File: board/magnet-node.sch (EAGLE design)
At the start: 30 parts, among them X1 SMA-142-0701-801/806, X2 SMA-142-0711-821/826

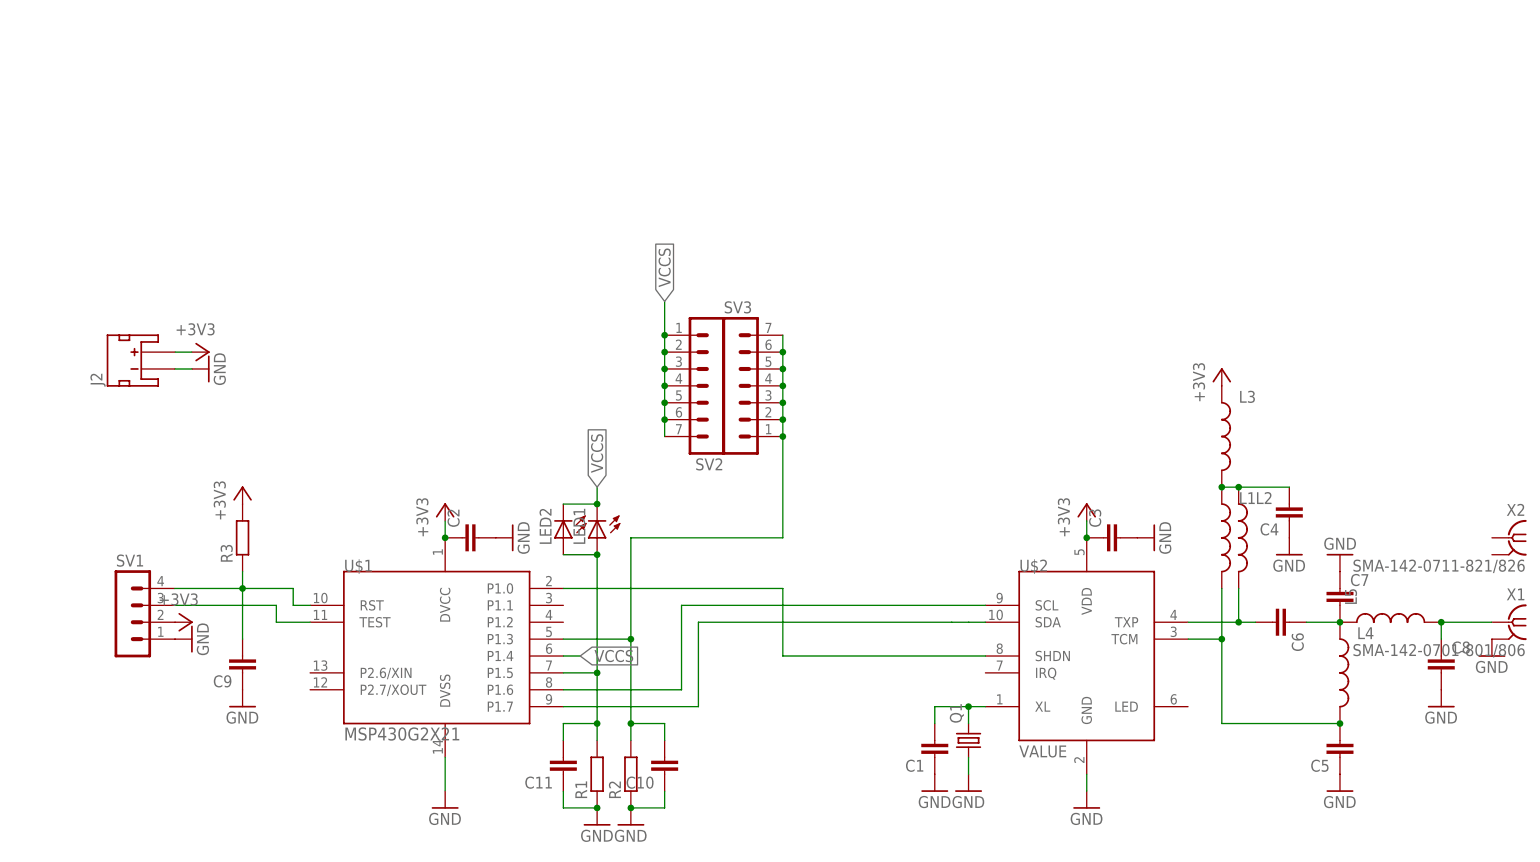
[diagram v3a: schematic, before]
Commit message: added temp/humid sensor
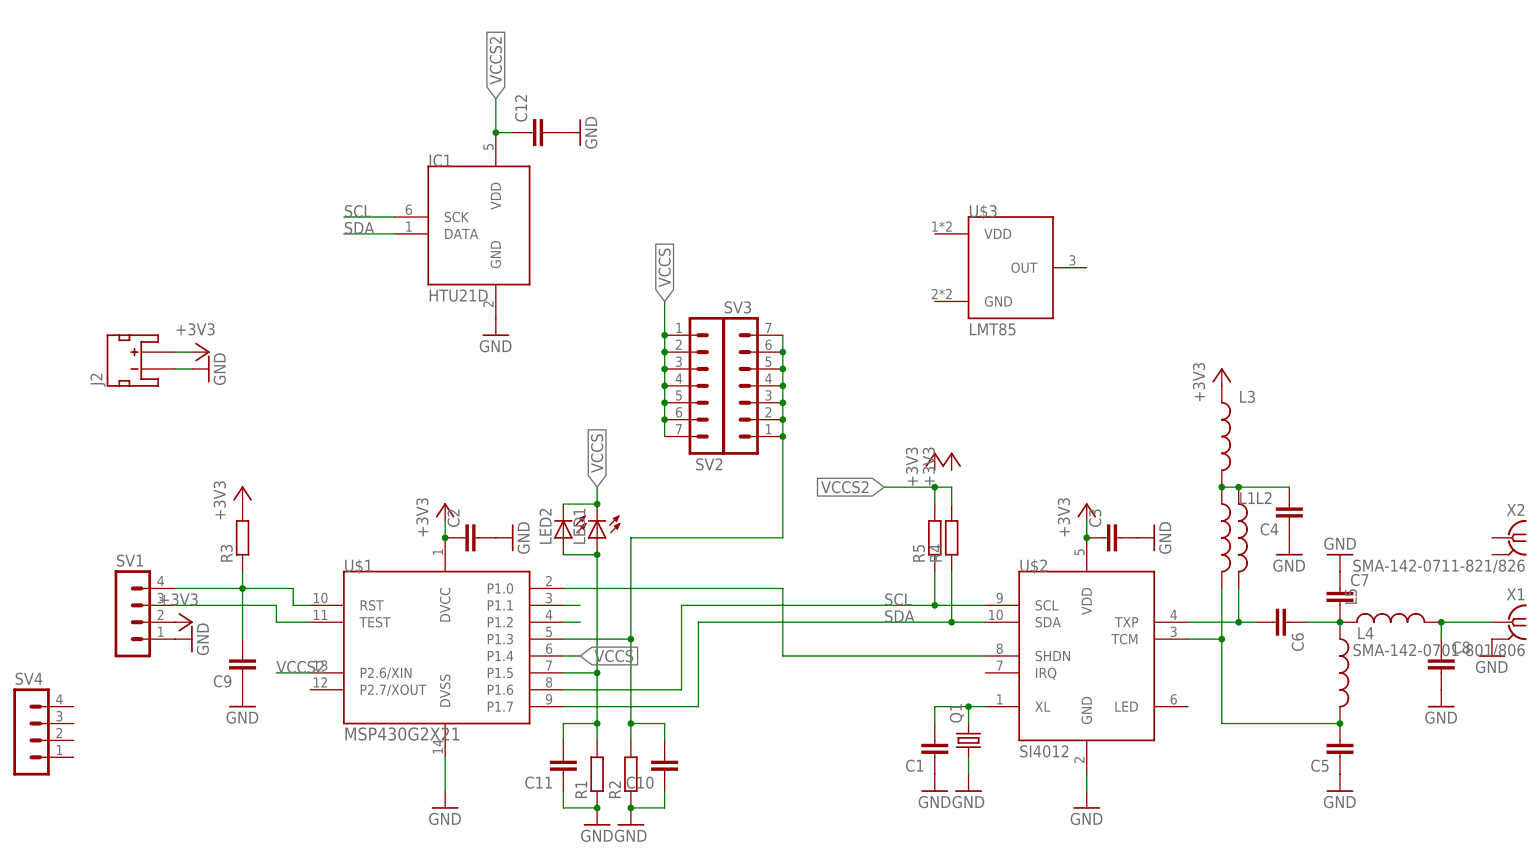
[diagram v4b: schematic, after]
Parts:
- added C12: (no value), rcl:C-EUC0603
- added IC1: HTU21D, Mine:HTU21D
- added R4, R5: (no value), rcl:R-EU_R0603
- added SV4: (no value), Mine:MA04-1E
- added U$3: LMT85, Mine:LMT85
- SV1: device con-lstb:MA04-1 -> Mine:MA04-1E
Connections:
- removed net N$3: U$1.P1.6, U$2.SCL
- removed net N$6: U$1.P1.7, U$2.SDA
- new net N$11: U$1.P1.1
- new net N$14: U$1.P1.2
- new net SCL: IC1.SCK, R5.1, U$1.P1.6, U$2.SCL
- new net SDA: IC1.DATA, R4.1, U$1.P1.7, U$2.SDA
- new net VCCS2: C12.1, IC1.VDD, R4.2, R5.2, U$1.P2.6/XIN
- net GND: now also C12.2, IC1.GND
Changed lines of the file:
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@@
 <part name="GND3" library="supply1" deviceset="GND" device=""/>
 <part name="GND4" library="supply1" deviceset="GND" device=""/>
-<part name="SV1" library="con-lstb" deviceset="MA04-1" device=""/>
+<part name="SV1" library="Mine" deviceset="MA04-1" device="E"/>
 <part name="+3V3" library="supply1" deviceset="+3V3" device=""/>
 <part name="GND5" library="supply1" deviceset="GND" device=""/>
@@
 <part name="X2" library="con-coax" deviceset="SMA-" device="142-0711-821/826"/>
 <part name="LED2" library="led" deviceset="LED" device="SMT1206"/>
+<part name="U$3" library="Mine" deviceset="LMT85" device=""/>
+<part name="IC1" library="Mine" deviceset="HTU21D" device=""/>
+<part name="SV4" library="Mine" deviceset="MA04-1" device="E"/>
+<part name="GND17" library="supply1" deviceset="GND" device=""/>
+<part name="C12" library="rcl" deviceset="C-EU" device="C0603"/>
+<part name="GND18" library="supply1" deviceset="GND" device=""/>
+<part name="R4" library="rcl" deviceset="R-EU_" device="R0603"/>
+<part name="R5" library="rcl" deviceset="R-EU_" device="R0603"/>
+<part name="+3V7" library="supply1" deviceset="+3V3" device=""/>
+<part name="+3V9" library="supply1" deviceset="+3V3" device=""/>
 </parts>
 <sheets>
@@
 <instance part="X2" gate="G1" x="205.74" y="58.42" rot="MR0"/>
 <instance part="LED2" gate="G$1" x="63.5" y="58.42" rot="R180"/>
+<instance part="U$3" gate="G$1" x="134.62" y="99.06"/>
+<instance part="IC1" gate="G$1" x="48.26" y="104.14"/>
+<instance part="SV4" gate="1" x="-17.78" y="30.48"/>
+<instance part="GND17" gate="1" x="53.34" y="88.9"/>
+<instance part="C12" gate="G$1" x="58.42" y="119.38" rot="R90"/>
+<instance part="GND18" gate="1" x="66.04" y="119.38" rot="R90"/>
+<instance part="R4" gate="G$1" x="121.92" y="58.42" rot="R90"/>
+<instance part="R5" gate="G$1" x="119.38" y="58.42" rot="R90"/>
+<instance part="+3V7" gate="G$1" x="121.92" y="71.12"/>
+<instance part="+3V9" gate="G$1" x="119.38" y="71.12"/>
 </instances>
 <busses>
@@
 <pinref part="GND16" gate="1" pin="GND"/>
 </segment>
+<segment>
+<pinref part="IC1" gate="G$1" pin="GND"/>
+<pinref part="GND17" gate="1" pin="GND"/>
+</segment>
+<segment>
+<pinref part="C12" gate="G$1" pin="2"/>
+<pinref part="GND18" gate="1" pin="GND"/>
+</segment>
 </net>
 <net name="+3V3" class="0">
@@
 </segment>
 </net>
-<net name="N$3" class="0">
+<net name="SCL" class="0">
 <segment>
 <pinref part="U$2" gate="G$1" pin="SCL"/>
-<wire x1="127" y1="48.26" x2="81.28" y2="48.26" width="0.1524" layer="91"/>
+<wire x1="127" y1="48.26" x2="119.38" y2="48.26" width="0.1524" layer="91"/>
+<wire x1="119.38" y1="48.26" x2="81.28" y2="48.26" width="0.1524" layer="91"/>
 <wire x1="81.28" y1="48.26" x2="81.28" y2="35.56" width="0.1524" layer="91"/>
 <pinref part="U$1" gate="G$1" pin="P1.6"/>
 <wire x1="81.28" y1="35.56" x2="63.5" y2="35.56" width="0.1524" layer="91"/>
+<label x="111.76" y="48.26" size="1.778" layer="95"/>
+<pinref part="R5" gate="G$1" pin="1"/>
+<wire x1="119.38" y1="53.34" x2="119.38" y2="48.26" width="0.1524" layer="91"/>
+<junction x="119.38" y="48.26"/>
+</segment>
+<segment>
+<pinref part="IC1" gate="G$1" pin="SCK"/>
+<wire x1="38.1" y1="106.68" x2="30.48" y2="106.68" width="0.1524" layer="91"/>
+<label x="30.48" y="106.68" size="1.778" layer="95"/>
 </segment>
 </net>
@@
 </segment>
 </net>
-<net name="N$6" class="0">
+<net name="SDA" class="0">
 <segment>
 <wire x1="83.82" y1="45.72" x2="121.92" y2="45.72" width="0.1524" layer="91"/>
-<wire x1="121.92" y1="45.72" x2="124.46" y2="45.72" width="0.1524" layer="91"/>
 <wire x1="83.82" y1="33.02" x2="83.82" y2="45.72" width="0.1524" layer="91"/>
 <pinref part="U$1" gate="G$1" pin="P1.7"/>
 <wire x1="63.5" y1="33.02" x2="83.82" y2="33.02" width="0.1524" layer="91"/>
 <pinref part="U$2" gate="G$1" pin="SDA"/>
-<wire x1="127" y1="45.72" x2="124.46" y2="45.72" width="0.1524" layer="91"/>
+<wire x1="127" y1="45.72" x2="121.92" y2="45.72" width="0.1524" layer="91"/>
+<label x="111.76" y="45.72" size="1.778" layer="95"/>
+<pinref part="R4" gate="G$1" pin="1"/>
+<wire x1="121.92" y1="53.34" x2="121.92" y2="45.72" width="0.1524" layer="91"/>
+<junction x="121.92" y="45.72"/>
+</segment>
+<segment>
+<pinref part="IC1" gate="G$1" pin="DATA"/>
+<wire x1="38.1" y1="104.14" x2="30.48" y2="104.14" width="0.1524" layer="91"/>
+<label x="30.48" y="104.14" size="1.778" layer="95"/>
 </segment>
 </net>
@@
 </segment>
 </net>
+<net name="N$11" class="0">
+<segment>
+<pinref part="U$1" gate="G$1" pin="P1.1"/>
+<wire x1="63.5" y1="48.26" x2="66.04" y2="48.26" width="0.1524" layer="91"/>
+</segment>
+</net>
+<net name="N$14" class="0">
+<segment>
+<pinref part="U$1" gate="G$1" pin="P1.2"/>
+<wire x1="66.04" y1="45.72" x2="63.5" y2="45.72" width="0.1524" layer="91"/>
+</segment>
+</net>
+<net name="VCCS2" class="0">
+<segment>
+<pinref part="U$1" gate="G$1" pin="P2.6/XIN"/>
+<wire x1="25.4" y1="38.1" x2="20.32" y2="38.1" width="0.1524" layer="91"/>
+<label x="20.32" y="38.1" size="1.778" layer="95"/>
+</segment>
+<segment>
+<pinref part="C12" gate="G$1" pin="1"/>
+<wire x1="55.88" y1="119.38" x2="53.34" y2="119.38" width="0.1524" layer="91"/>
+<wire x1="53.34" y1="119.38" x2="53.34" y2="124.46" width="0.1524" layer="91"/>
+<label x="53.34" y="124.46" size="1.778" layer="95" rot="R90" xref="yes"/>
+<pinref part="IC1" gate="G$1" pin="VDD"/>
+<junction x="53.34" y="119.38"/>
+</segment>
+<segment>
+<pinref part="R4" gate="G$1" pin="2"/>
+<wire x1="121.92" y1="63.5" x2="121.92" y2="66.04" width="0.1524" layer="91"/>
+<wire x1="121.92" y1="66.04" x2="119.38" y2="66.04" width="0.1524" layer="91"/>
+<pinref part="R5" gate="G$1" pin="2"/>
+<wire x1="119.38" y1="66.04" x2="111.76" y2="66.04" width="0.1524" layer="91"/>
+<wire x1="119.38" y1="63.5" x2="119.38" y2="66.04" width="0.1524" layer="91"/>
+<label x="111.76" y="66.04" size="1.778" layer="95" rot="R180" xref="yes"/>
+<junction x="119.38" y="66.04"/>
+</segment>
+</net>

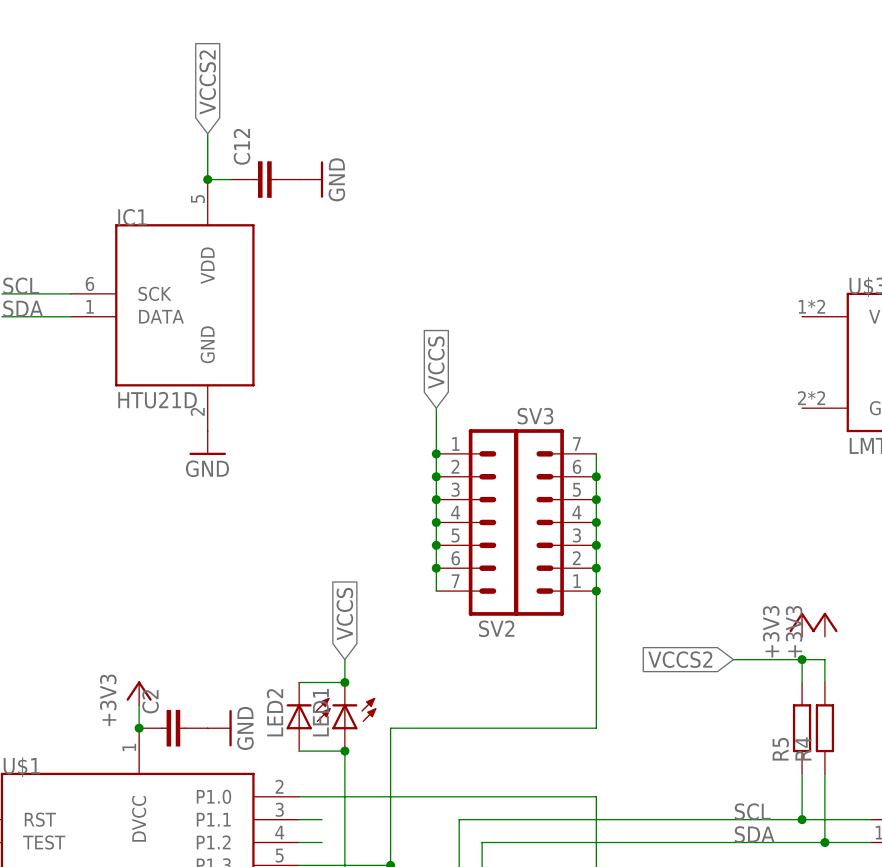
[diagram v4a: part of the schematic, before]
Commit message: started mppt modelling
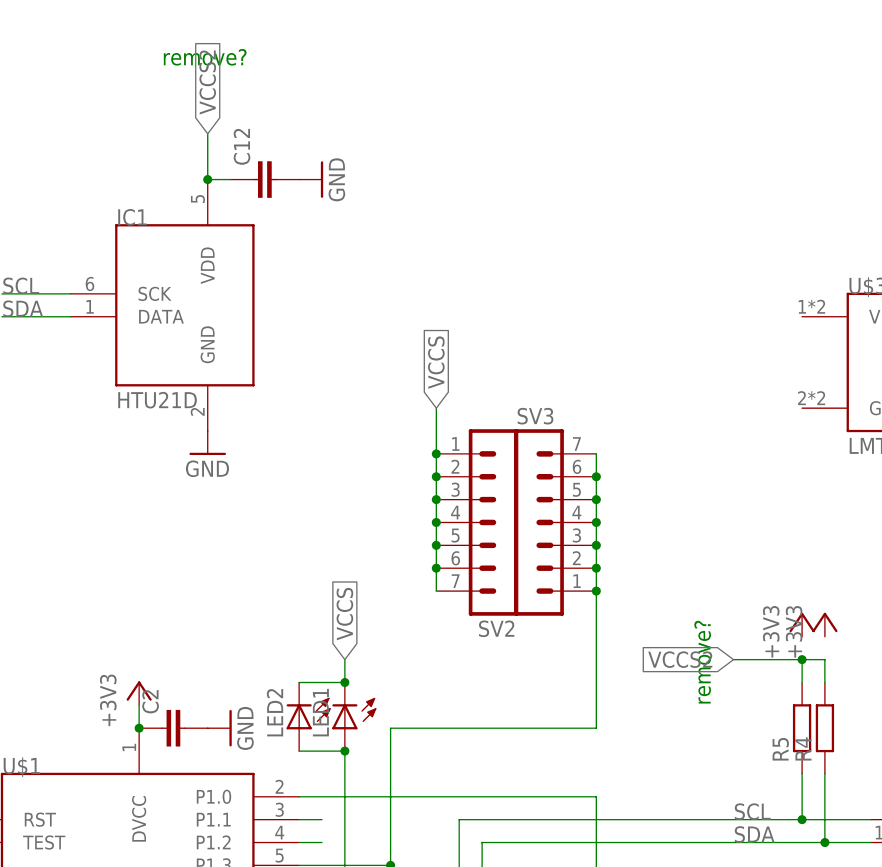
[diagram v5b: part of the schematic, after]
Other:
- note added: "remove?"
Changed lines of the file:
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@@
 <sheet>
 <plain>
+<text x="48.26" y="132.08" size="1.778" layer="91">remove?</text>
+<text x="109.22" y="60.96" size="1.778" layer="91" rot="R90">remove?</text>
 </plain>
 <instances>

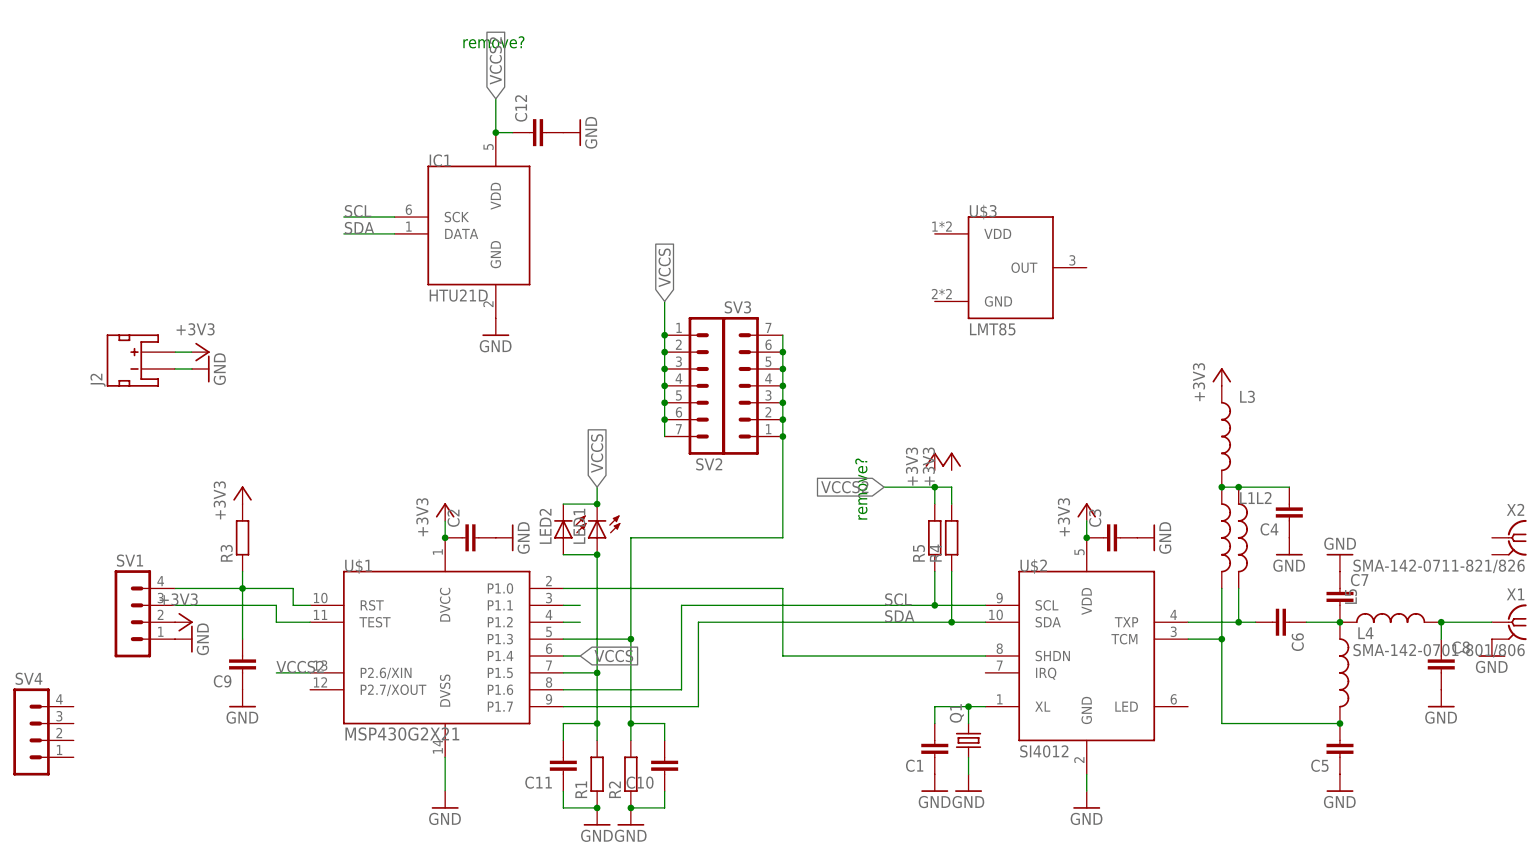
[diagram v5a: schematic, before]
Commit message: changed footprints in magnet node
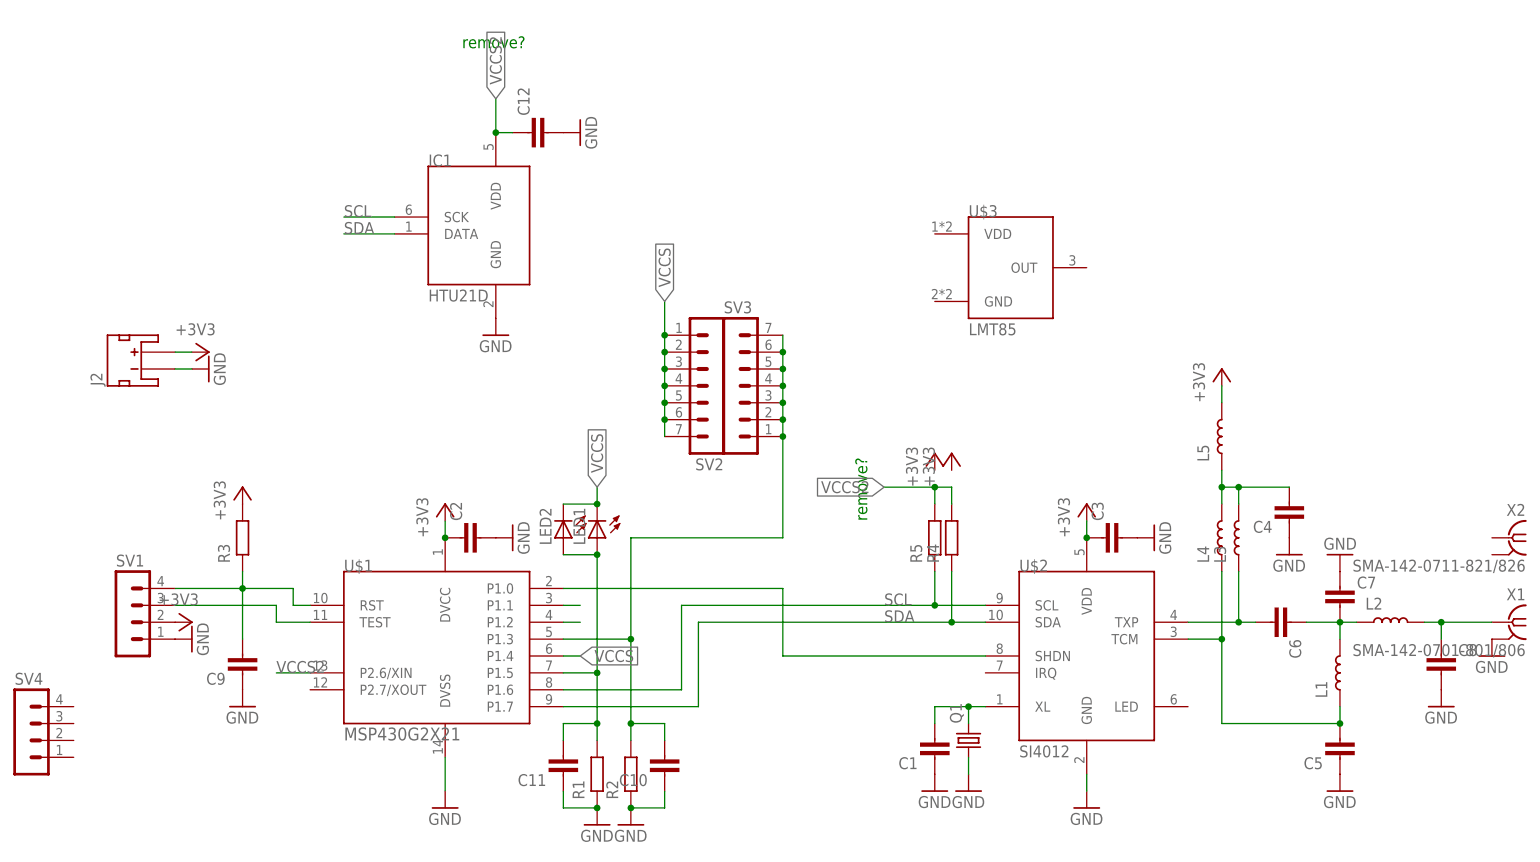
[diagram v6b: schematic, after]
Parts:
- C1, C10, C11, C12, C2, C3, C4, C5, C6, C7, C8, C9: device rcl:C-EUC0603 -> passives-7351:CAPACITOR0603-N
- L1, L2, L3, L4, L5: device SparkFun-Passives:INDUCTOR0402 -> passives-7351:INDUCTOR0402-N
- R1, R2, R3, R4, R5: device rcl:R-EU_R0603 -> passives-7351:RESISTOR0603-N
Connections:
- net +3V3: now also L5.P$2, R3.P$2; no longer L3.1, R3.2
- net GND: now also R1.P$1, R2.P$1; no longer R1.1, R2.1
- net N$10: now also L2.P$2; no longer L5.2
- net N$12: now also R2.P$2; no longer R2.2
- net N$13: now also R1.P$2; no longer R1.2
- net N$15: now also R3.P$1; no longer R3.1
- net N$4: now also L3.P$2, L4.P$2, L5.P$1; no longer L1.1, L2.1, L3.2
- net N$7: now also L1.P$2, L2.P$1; no longer L4.1, L5.1
- net N$8: now also L1.P$1, L4.P$1; no longer L1.2, L4.2
- net N$9: now also L3.P$1; no longer L2.2
- net SCL: now also R5.P$1; no longer R5.1
- net SDA: now also R4.P$1; no longer R4.1
- net VCCS2: now also R4.P$2, R5.P$2; no longer R4.2, R5.2
